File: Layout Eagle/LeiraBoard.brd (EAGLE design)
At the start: 47.9 x 39.4 mm, 5 parts

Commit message: Atualização LeiraBoard
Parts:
- removed PINOS_UMIDADE: (no value), con-lstb:MA03-1
- added SV1: (no value), con-lstb:MA04-1
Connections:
- net ANA_UMIDADE: now also SV1.1; no longer PINOS_UMIDADE.2
- net GND: now also SV1.3; no longer PINOS_UMIDADE.1
- net VCC: now also SV1.4; no longer PINOS_UMIDADE.3
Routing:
- net GND: track 83.0 -> 90.0 mm
- net ANA_METANO: track 23.4 -> 17.2 mm
- net ANA_UMIDADE: track 13.0 -> 11.4 mm
- net VCC: track 76.3 -> 75.5 mm
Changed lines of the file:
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@@
 <attribute name="OC_NEWARK" value="unknown" x="5.08" y="36.195" size="1.778" layer="27" rot="R90" display="off"/>
 </element>
-<element name="PINOS_UMIDADE" library="con-lstb" library_urn="urn:adsk.eagle:library:162" package="MA03-1" package3d_urn="urn:adsk.eagle:package:8339/1" value="" x="0.635" y="22.86" rot="R90">
-<attribute name="MF" value="" x="0.635" y="22.86" size="1.778" layer="27" rot="R90" display="off"/>
-<attribute name="MPN" value="" x="0.635" y="22.86" size="1.778" layer="27" rot="R90" display="off"/>
-<attribute name="OC_FARNELL" value="unknown" x="0.635" y="22.86" size="1.778" layer="27" rot="R90" display="off"/>
-<attribute name="OC_NEWARK" value="unknown" x="0.635" y="22.86" size="1.778" layer="27" rot="R90" display="off"/>
+<element name="U$1" library="Geisa" package="DIL8" value="ADC8032" x="17.145" y="17.145" rot="R270"/>
+<element name="SV1" library="con-lstb" library_urn="urn:adsk.eagle:library:162" package="MA04-1" package3d_urn="urn:adsk.eagle:package:8337/1" value="" x="1.905" y="19.685" rot="R270">
+<attribute name="MF" value="" x="1.905" y="19.685" size="1.778" layer="27" rot="R270" display="off"/>
+<attribute name="MPN" value="" x="1.905" y="19.685" size="1.778" layer="27" rot="R270" display="off"/>
+<attribute name="OC_FARNELL" value="unknown" x="1.905" y="19.685" size="1.778" layer="27" rot="R270" display="off"/>
+<attribute name="OC_NEWARK" value="unknown" x="1.905" y="19.685" size="1.778" layer="27" rot="R270" display="off"/>
 </element>
-<element name="U$1" library="Geisa" package="DIL8" value="ADC8032" x="17.145" y="17.145" rot="R270"/>
 </elements>
 <signals>
@@
 <contactref element="J1" pad="1"/>
 <contactref element="PINOS_METANO" pad="3"/>
-<contactref element="PINOS_UMIDADE" pad="3"/>
 <contactref element="PINOS_TEMPERATURA" pad="3"/>
 <wire x1="20.955" y1="26.035" x2="21.2725" y2="25.7175" width="1.016" layer="16"/>
@@
 <wire x1="33.3375" y1="16.1925" x2="33.02" y2="16.1925" width="1.016" layer="16"/>
 <wire x1="33.3375" y1="16.1925" x2="33.505" y2="16.05" width="1.016" layer="16"/>
-<wire x1="3.81" y1="13.97" x2="5.08" y2="12.7" width="1.016" layer="1"/>
-<wire x1="3.81" y1="23.8125" x2="3.81" y2="13.97" width="1.016" layer="1"/>
-<wire x1="2.2225" y1="25.4" x2="3.81" y2="23.8125" width="1.016" layer="1"/>
-<wire x1="0.635" y1="25.4" x2="2.2225" y2="25.4" width="1.016" layer="1"/>
-<wire x1="0.635" y1="25.4" x2="1.905" y2="25.7175" width="1.016" layer="1"/>
-<wire x1="0.635" y1="25.4" x2="6.35" y2="31.115" width="1.016" layer="16"/>
-<wire x1="1.905" y1="38.1" x2="2.54" y2="38.735" width="1.016" layer="1"/>
-<wire x1="2.54" y1="38.735" x2="5.08" y2="38.735" width="1.016" layer="1"/>
-<wire x1="1.905" y1="25.7175" x2="1.905" y2="38.1" width="1.016" layer="1"/>
-<wire x1="19.685" y1="31.115" x2="20.955" y2="29.845" width="1.016" layer="16"/>
+<wire x1="20.955" y1="29.845" x2="19.685" y2="31.115" width="1.016" layer="16"/>
 <wire x1="20.955" y1="29.845" x2="20.955" y2="26.035" width="1.016" layer="16"/>
-<wire x1="6.35" y1="31.115" x2="19.685" y2="31.115" width="1.016" layer="16"/>
+<contactref element="SV1" pad="4"/>
+<wire x1="2.54" y1="31.115" x2="0" y2="33.655" width="1.016" layer="16"/>
+<wire x1="0" y1="33.655" x2="0" y2="36.83" width="1.016" layer="16"/>
+<wire x1="0" y1="36.83" x2="1.905" y2="38.735" width="1.016" layer="16"/>
+<wire x1="19.685" y1="31.115" x2="2.54" y2="31.115" width="1.016" layer="16"/>
+<wire x1="-1.143" y1="17.5733125" x2="-1.143" y2="17.653" width="1.016" layer="16"/>
+<wire x1="-1.143" y1="17.653" x2="-1.27" y2="17.78" width="1.016" layer="16"/>
+<wire x1="0.5553125" y1="15.875" x2="1.905" y2="15.875" width="1.016" layer="16"/>
+<wire x1="0.5553125" y1="15.875" x2="-1.143" y2="17.5733125" width="1.016" layer="16"/>
+<wire x1="-1.27" y1="17.78" x2="-1.27" y2="27.305" width="1.016" layer="16"/>
+<wire x1="-1.27" y1="27.305" x2="2.54" y2="31.115" width="1.016" layer="16"/>
+<wire x1="1.905" y1="15.875" x2="5.08" y2="12.7" width="1.016" layer="16"/>
+<wire x1="1.905" y1="38.735" x2="5.08" y2="38.735" width="1.016" layer="16"/>
 </signal>
 <signal name="ADC_CLK">
@@
 <signal name="ANA_UMIDADE">
 <contactref element="U$1" pad="2"/>
-<contactref element="PINOS_UMIDADE" pad="2"/>
-<wire x1="12.7" y1="22.86" x2="13.335" y2="23.495" width="0.508" layer="16"/>
-<wire x1="0.635" y1="22.86" x2="12.7" y2="22.86" width="0.508" layer="16"/>
+<contactref element="SV1" pad="1"/>
+<wire x1="13.335" y1="23.495" x2="1.905" y2="23.495" width="0.508" layer="16"/>
 </signal>
 <signal name="ANA_METANO">
 <contactref element="U$1" pad="3"/>
 <contactref element="PINOS_METANO" pad="2"/>
-<wire x1="13.97" y1="20.32" x2="13.335" y2="20.955" width="0.508" layer="16"/>
-<wire x1="14.9225" y1="20.32" x2="13.97" y2="20.32" width="0.508" layer="16"/>
-<wire x1="14.9225" y1="20.32" x2="16.1925" y2="19.05" width="0.508" layer="16"/>
-<wire x1="12.7" y1="10.16" x2="5.08" y2="10.16" width="0.508" layer="16"/>
-<wire x1="12.7" y1="10.16" x2="13.0175" y2="10.16" width="0.508" layer="16"/>
-<wire x1="16.1925" y1="19.05" x2="16.1925" y2="11.1125" width="0.508" layer="16"/>
-<wire x1="16.1925" y1="11.1125" x2="15.24" y2="10.16" width="0.508" layer="16"/>
-<wire x1="15.24" y1="10.16" x2="12.7" y2="10.16" width="0.508" layer="16"/>
+<wire x1="13.335" y1="20.955" x2="10.16" y2="20.955" width="0.508" layer="16"/>
+<wire x1="10.16" y1="20.955" x2="9.525" y2="20.32" width="0.508" layer="16"/>
+<wire x1="9.525" y1="20.32" x2="9.525" y2="12.7" width="0.508" layer="16"/>
+<wire x1="9.525" y1="12.7" x2="6.985" y2="10.16" width="0.508" layer="16"/>
+<wire x1="6.985" y1="10.16" x2="5.08" y2="10.16" width="0.508" layer="16"/>
 </signal>
 <signal name="ADC_/CS">
@@
 <contactref element="U$1" pad="4"/>
 <contactref element="J1" pad="5"/>
-<contactref element="PINOS_UMIDADE" pad="1"/>
 <contactref element="PINOS_METANO" pad="1"/>
 <contactref element="PINOS_TEMPERATURA" pad="1"/>
-<wire x1="13.0175" y1="18.7325" x2="13.335" y2="18.415" width="1.016" layer="16"/>
-<wire x1="2.2225" y1="18.7325" x2="13.0175" y2="18.7325" width="1.016" layer="16"/>
-<wire x1="2.2225" y1="18.7325" x2="0.635" y2="20.32" width="1.016" layer="16"/>
-<wire x1="0.635" y1="8.89" x2="0.635" y2="20.32" width="1.016" layer="1"/>
-<wire x1="0.3175" y1="20.6375" x2="0.635" y2="20.32" width="1.016" layer="16"/>
 <wire x1="27.305" y1="33.3375" x2="33.3375" y2="27.305" width="1.016" layer="16"/>
 <wire x1="5.3975" y1="33.3375" x2="27.305" y2="33.3375" width="1.016" layer="16"/>
 <wire x1="33.3375" y1="27.305" x2="33.505" y2="27.13" width="1.016" layer="16"/>
-<wire x1="5.08" y1="7.62" x2="1.905" y2="7.62" width="1.016" layer="1"/>
-<wire x1="1.905" y1="7.62" x2="0.635" y2="8.89" width="1.016" layer="1"/>
-<wire x1="-2.54" y1="29.845" x2="1.27" y2="33.655" width="1.016" layer="16"/>
-<wire x1="1.27" y1="33.655" x2="5.08" y2="33.655" width="1.016" layer="16"/>
 <wire x1="5.08" y1="33.655" x2="5.3975" y2="33.3375" width="1.016" layer="16"/>
-<wire x1="0.635" y1="20.32" x2="-1.905" y2="20.32" width="1.016" layer="16"/>
-<wire x1="-1.905" y1="20.32" x2="-2.54" y2="20.955" width="1.016" layer="16"/>
-<wire x1="-2.54" y1="20.955" x2="-2.54" y2="29.845" width="1.016" layer="16"/>
+<contactref element="SV1" pad="3"/>
+<wire x1="5.08" y1="33.655" x2="1.27" y2="33.655" width="1.016" layer="1"/>
+<wire x1="1.27" y1="33.655" x2="-2.54" y2="29.845" width="1.016" layer="1"/>
+<wire x1="-2.54" y1="29.845" x2="-2.54" y2="20.955" width="1.016" layer="1"/>
+<wire x1="-2.54" y1="20.955" x2="0" y2="18.415" width="1.016" layer="1"/>
+<wire x1="0" y1="18.415" x2="1.905" y2="18.415" width="1.016" layer="1"/>
+<wire x1="-1.143" y1="16.7166875" x2="-1.143" y2="16.637" width="1.016" layer="1"/>
+<wire x1="-1.143" y1="16.637" x2="-1.27" y2="16.51" width="1.016" layer="1"/>
+<wire x1="1.905" y1="18.415" x2="0.5553125" y2="18.415" width="1.016" layer="1"/>
+<wire x1="0.5553125" y1="18.415" x2="-1.143" y2="16.7166875" width="1.016" layer="1"/>
+<wire x1="-1.27" y1="16.51" x2="-1.27" y2="10.16" width="1.016" layer="1"/>
+<wire x1="-1.27" y1="10.16" x2="1.27" y2="7.62" width="1.016" layer="1"/>
+<wire x1="1.27" y1="7.62" x2="5.08" y2="7.62" width="1.016" layer="1"/>
+<wire x1="13.335" y1="18.415" x2="13.335" y2="10.16" width="1.016" layer="16"/>
+<wire x1="13.335" y1="10.16" x2="10.795" y2="7.62" width="1.016" layer="16"/>
+<wire x1="10.795" y1="7.62" x2="5.08" y2="7.62" width="1.016" layer="16"/>
 </signal>
 <signal name="TEMPERATURA">

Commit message: LeiraBoard Atualizada
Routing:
- net ADC_/CS: track 23.9 -> 25.3 mm
- added copper zone on layer 1, net GND
- added copper zone on layer 16, net VCC

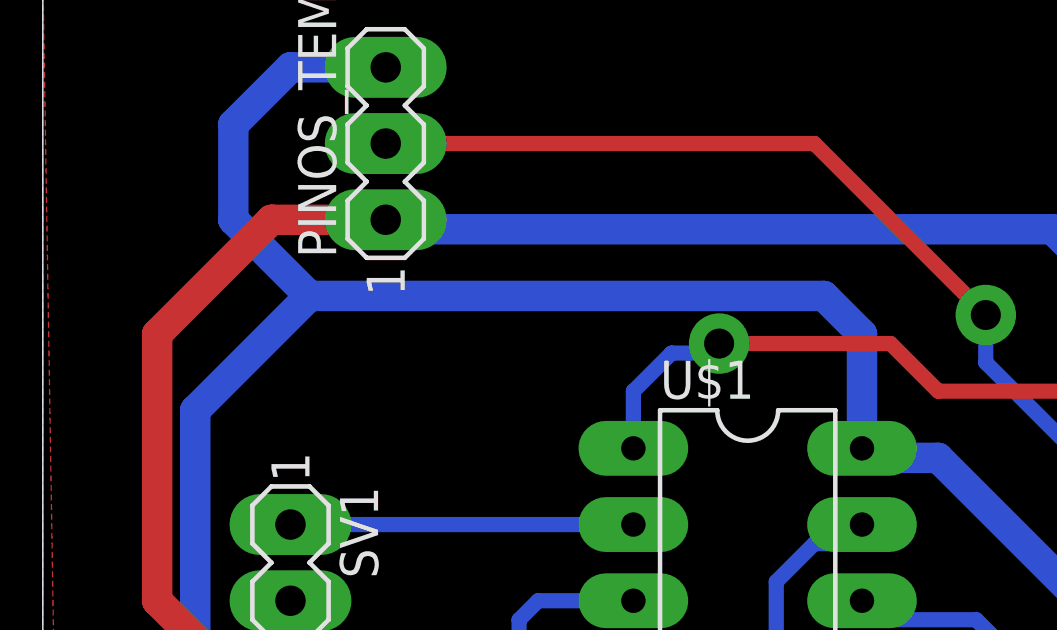
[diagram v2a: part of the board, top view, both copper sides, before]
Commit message: Detalhe do bottom consertado
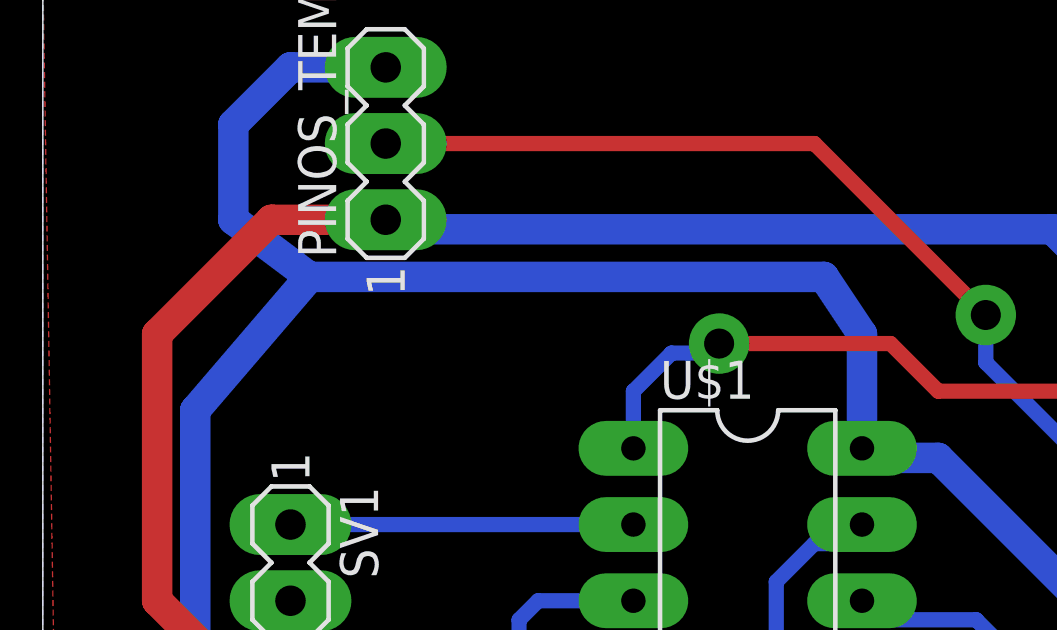
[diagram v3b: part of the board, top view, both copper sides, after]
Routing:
- net VCC: track 75.5 -> 76.0 mm
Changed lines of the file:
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@@
 <grid distance="25" unitdist="mil" unit="mil" style="lines" multiple="1" display="no" altdistance="5" altunitdist="mil" altunit="mil"/>
 <layers>
-<layer number="1" name="Top" color="4" fill="1" visible="yes" active="yes"/>
+<layer number="1" name="Top" color="4" fill="1" visible="no" active="yes"/>
 <layer number="16" name="Bottom" color="1" fill="1" visible="yes" active="yes"/>
 <layer number="17" name="Pads" color="2" fill="1" visible="yes" active="yes"/>
@@
 <wire x1="33.3375" y1="16.1925" x2="33.02" y2="16.1925" width="1.016" layer="16"/>
 <wire x1="33.3375" y1="16.1925" x2="33.505" y2="16.05" width="1.016" layer="16"/>
-<wire x1="20.955" y1="29.845" x2="19.685" y2="31.115" width="1.016" layer="16"/>
+<wire x1="20.955" y1="29.845" x2="19.685" y2="31.75" width="1.016" layer="16"/>
 <wire x1="20.955" y1="29.845" x2="20.955" y2="26.035" width="1.016" layer="16"/>
 <contactref element="SV1" pad="4"/>
-<wire x1="2.54" y1="31.115" x2="0" y2="33.655" width="1.016" layer="16"/>
+<wire x1="2.54" y1="31.75" x2="0" y2="33.655" width="1.016" layer="16"/>
 <wire x1="0" y1="33.655" x2="0" y2="36.83" width="1.016" layer="16"/>
 <wire x1="0" y1="36.83" x2="1.905" y2="38.735" width="1.016" layer="16"/>
-<wire x1="19.685" y1="31.115" x2="2.54" y2="31.115" width="1.016" layer="16"/>
+<wire x1="19.685" y1="31.75" x2="2.54" y2="31.75" width="1.016" layer="16"/>
 <wire x1="-1.143" y1="17.5733125" x2="-1.143" y2="17.653" width="1.016" layer="16"/>
 <wire x1="-1.143" y1="17.653" x2="-1.27" y2="17.78" width="1.016" layer="16"/>
@@
 <wire x1="0.5553125" y1="15.875" x2="-1.143" y2="17.5733125" width="1.016" layer="16"/>
 <wire x1="-1.27" y1="17.78" x2="-1.27" y2="27.305" width="1.016" layer="16"/>
-<wire x1="-1.27" y1="27.305" x2="2.54" y2="31.115" width="1.016" layer="16"/>
+<wire x1="-1.27" y1="27.305" x2="2.54" y2="31.75" width="1.016" layer="16"/>
 <wire x1="1.905" y1="15.875" x2="5.08" y2="12.7" width="1.016" layer="16"/>
 <wire x1="1.905" y1="38.735" x2="5.08" y2="38.735" width="1.016" layer="16"/>
